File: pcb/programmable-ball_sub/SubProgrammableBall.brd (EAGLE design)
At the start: 20.5 x 20 mm, 9 parts, among them CON1 B4B-ZR-SM4-TF, U2 LSM6DS0TR

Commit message: brd, schの更新
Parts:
- moved FB1 11.1 mm to (16.5, 8.62), turned to 180 degrees
- moved R2 8.52 mm to (11.4, 15.2), turned to 90 degrees
- moved R3 8.13 mm to (8.89, 15.2), turned to 90 degrees
- moved C1 5.24 mm to (15.2, 14.0)
- moved R4 5.24 mm to (5.08, 14.0), turned to 90 degrees
- moved R1 3.79 mm to (6.35, 11.2)
- moved U2 0.22 mm to (9.96, 10.1), turned to 270 degrees
- moved CON1 0.21 mm to (9.98, 5.34)
- turned C2 to 180 degrees
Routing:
- net +3V3: track 0.00 -> 32.0 mm, vias 0 -> 2
- net N$3: track 0.00 -> 15.1 mm, vias 0 -> 2
- net SCL: track 0.00 -> 14.0 mm, vias 0 -> 2
- net N$1: track 0.00 -> 9.78 mm
- net N$5: track 0.00 -> 5.66 mm
- net N$2: track 0.00 -> 1.82 mm
- added copper zone on layer 1, net GND
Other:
- board size 20.5 x 20 mm -> 20 x 20 mm

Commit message: ベタ変更
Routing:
- net GND: track 0.00 -> 16.3 mm, vias 0 -> 2
- net +3V3: track 32.0 -> 47.3 mm, vias 2 -> 3
- net SCL: track 14.0 -> 25.5 mm, vias 2 -> 0
- net N$3: track 15.1 -> 20.3 mm, vias 2 -> 0
- net N$1: track 9.78 -> 8.54 mm
- added copper zone on layer 16, net GND

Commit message: 軽微な修正
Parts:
- moved C1 2.58 mm to (13.7, 11.9), turned to 90 degrees
- moved FB1 1.55 mm to (15.0, 8.22)
- moved R4 1.30 mm to (6.18, 13.3), turned to 180 degrees
- moved C2 1.00 mm to (15.9, 12.2), turned to 90 degrees
- moved R2 0.64 mm to (11.0, 15.7)
- moved R3 0.51 mm to (8.79, 15.7)
- moved R1 0.22 mm to (6.15, 11.1)
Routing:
- net +3V3: track 47.3 -> 26.2 mm, vias 3 -> 2
- net N$3: track 20.3 -> 10.0 mm, vias 0 -> 2
- net SCL: track 25.5 -> 19.5 mm
- net GND: track 16.3 -> 21.3 mm
- net N$5: track 5.27 -> 3.39 mm
- net N$1: track 8.54 -> 7.49 mm

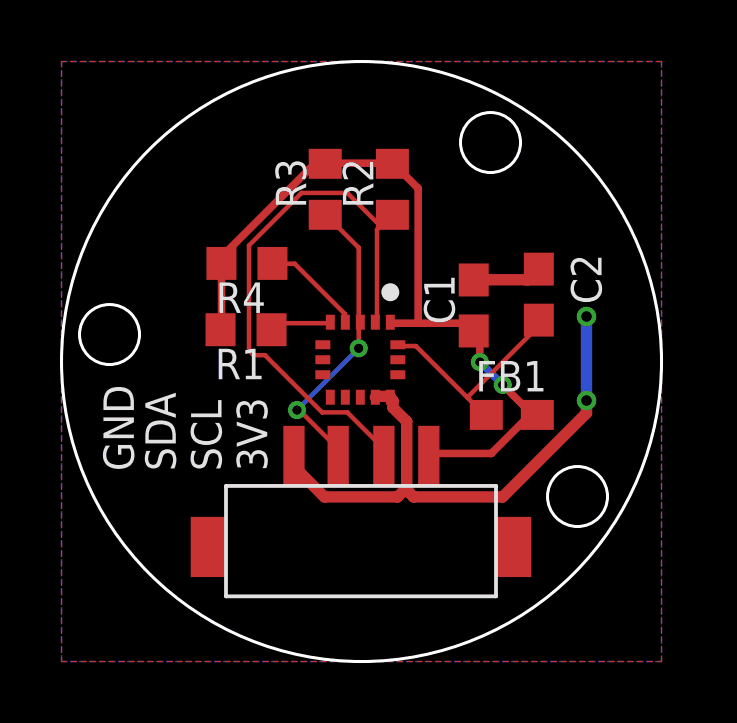
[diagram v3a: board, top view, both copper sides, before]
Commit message: 加速度センサのfoot print間違い修正
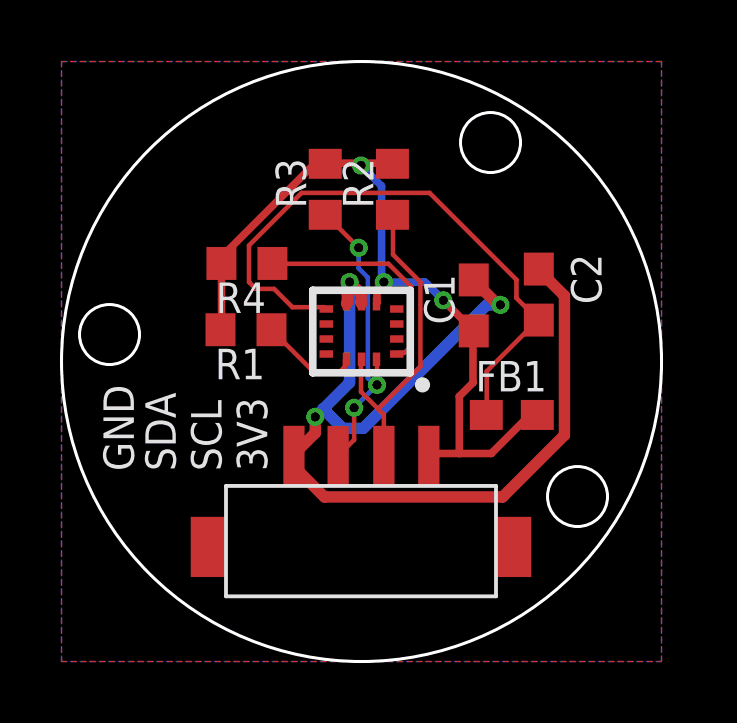
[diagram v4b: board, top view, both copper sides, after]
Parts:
- removed U2: LSM6DS0TR, SubProgrammableBall:PQFN50P300X300X86-16N
- added U3: LSM6DS0, temp:LGA14L
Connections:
- removed net N$2: R1.1, U2.5
- removed net N$3: CON1.3, R3.1, U2.3
- removed net N$5: R4.1, U2.4
- new net CS: R1.1, U3.12
- new net SD0: R4.1, U3.1
- new net SDA: CON1.3, R3.1, U3.14
- net +3V3: now also U3.5; no longer U2.1
- net GND: now also U3.6, U3.7; no longer U2.12, U2.13
- net N$1: now also U3.8; no longer U2.16
- net SCL: now also U3.13; no longer U2.2
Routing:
- net N$1: track 7.49 -> 20.6 mm
- net GND: track 21.3 -> 33.7 mm, vias 2 -> 3
- net SDA: track 0.00 -> 10.2 mm, vias 0 -> 3
- net N$3: track 10.0 -> 0.00 mm, vias 2 -> 0
- net SCL: track 19.5 -> 11.0 mm
- net SD0: track 0.00 -> 7.52 mm
- net CS: track 0.00 -> 3.43 mm
- net N$5: track 3.39 -> 0.00 mm
- net N$2: track 2.09 -> 0.00 mm
- net +3V3: track 26.2 -> 26.7 mm, vias 2 -> 3
